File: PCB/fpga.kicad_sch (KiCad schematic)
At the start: 76 parts, among them IC1 S25FL256LAGMFI003, J1 0878311420, J4 62684-402100ALF, U4 XC7A100T-FTG256, U5 IS62C1024AL-35QLI-TR, Y2 ECS-3953M-400-BN-TR

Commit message: Add
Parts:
- removed C24, C25, C26, C27, C28, C29, C43, C44, C50, C51, C61, C62, C68, C69, C75, C76, C82, C83: 4.7u, symbol Device:C
- removed C30, C31, C32, C33, C34, C35, C36, C38, C40, C41, C45, C46, C47, C52, C53, C54, C55, C56, C58, C59, C60, C64, C65, C66, C67, C71, C72, C73, C74, C78, C79, C80, C81: 470n, symbol Device:C
- removed C37: 330u, symbol Device:C
- removed C39: 100u, symbol Device:C
- removed C42, C48, C49, C63, C70, C77, C84: 47u, symbol Device:C
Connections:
- net GND: no longer U4.L4 (IO_L1P_T0_34), U4.L5 (IO_0_34), U4.M1 (IO_L2N_T0_34), U4.M2 (IO_L2P_T0_34), U4.M4 (IO_L1N_T0_34), U4.M5 (IO_L6P_T0_34), U4.N1 (IO_L4P_T0_34), U4.N2 (IO_L3N_T0_DQS_34), U4.N3 (IO_L3P_T0_DQS_34), U4.N4 (IO_L6N_T0_VREF_34), U4.P1 (IO_L4N_T0_34), U4.P3 (IO_L5N_T0_34), U4.P4 (IO_L5P_T0_34), U4.R1 (IO_L7N_T1_34), U4.R2 (IO_L7P_T1_34), U4.R3 (IO_L8P_T1_34), U4.T2 (IO_L8N_T1_34)
- new net BLUE0: U4.P3 (IO_L5N_T0_34)
- new net BLUE1: U4.M5 (IO_L6P_T0_34)
- new net BLUE2: U4.N4 (IO_L6N_T0_VREF_34)
- new net BLUE3: U4.R2 (IO_L7P_T1_34)
- new net BLUE4: U4.R1 (IO_L7N_T1_34)
- new net GREEN0: U4.N3 (IO_L3P_T0_DQS_34)
- new net GREEN1: U4.N2 (IO_L3N_T0_DQS_34)
- new net GREEN2: U4.N1 (IO_L4P_T0_34)
- new net GREEN3: U4.P1 (IO_L4N_T0_34)
- new net GREEN4: U4.P4 (IO_L5P_T0_34)
- new net HSYNC: U4.T2 (IO_L8N_T1_34)
- new net RED0: U4.L5 (IO_0_34)
- new net RED1: U4.L4 (IO_L1P_T0_34)
- new net RED2: U4.M4 (IO_L1N_T0_34)
- new net RED3: U4.M2 (IO_L2P_T0_34)
- new net RED4: U4.M1 (IO_L2N_T0_34)
- new net VSYNC: U4.R3 (IO_L8P_T1_34)
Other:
- moved on the sheet: J4, U4B, U4D

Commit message: pls work
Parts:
- C23, C57: value C -> 100n
- R13: value R -> 2.4k
- R14, R15, R18, R19: value R -> 4.7k
- R16, R17: value R -> 10k
- R20: value R -> 330
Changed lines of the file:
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@@
       (effects (font (size 1.27 1.27)) hide)
     )
-    (property "Value" "GND" (at 262.89 100.33 0)
+    (property "Value" "GND" (at 243.205 90.17 0)
       (effects (font (size 1.27 1.27)))
     )
@@
   )
   (symbol (lib_id "Device:C") (at 35.56 33.02 90) (unit 1)
-    (in_bom yes) (on_board yes) (dnp no) (fields_autoplaced)
-    (property "Reference" "C57" (at 35.56 25.4 90)
-      (effects (font (size 1.27 1.27)))
-    )
-    (property "Value" "C" (at 35.56 27.94 90)
+    (in_bom yes) (on_board yes) (dnp no)
+    (property "Reference" "C57" (at 35.56 26.67 90)
+      (effects (font (size 1.27 1.27)))
+    )
+    (property "Value" "100n" (at 35.56 29.21 90)
       (effects (font (size 1.27 1.27)))
     )
@@
       (effects (font (size 1.27 1.27)) (justify left))
     )
-    (property "Value" "C" (at 90.17 175.895 0)
+    (property "Value" "100n" (at 90.17 175.895 0)
       (effects (font (size 1.27 1.27)) (justify left))
     )
@@
   )
   (symbol (lib_id "Device:R") (at 33.02 105.41 180) (unit 1)
-    (in_bom yes) (on_board yes) (dnp no) (fields_autoplaced)
-    (property "Reference" "R16" (at 35.56 104.14 0)
+    (in_bom yes) (on_board yes) (dnp no)
+    (property "Reference" "R16" (at 31.115 99.695 0)
       (effects (font (size 1.27 1.27)) (justify right))
     )
-    (property "Value" "R" (at 35.56 106.68 0)
+    (property "Value" "10k" (at 33.02 107.315 90)
       (effects (font (size 1.27 1.27)) (justify right))
     )
@@
   )
   (symbol (lib_id "Device:R") (at 48.26 142.24 180) (unit 1)
-    (in_bom yes) (on_board yes) (dnp no) (fields_autoplaced)
-    (property "Reference" "R19" (at 50.8 140.97 0)
+    (in_bom yes) (on_board yes) (dnp no)
+    (property "Reference" "R19" (at 50.165 140.97 0)
       (effects (font (size 1.27 1.27)) (justify right))
     )
-    (property "Value" "R" (at 50.8 143.51 0)
+    (property "Value" "4.7k" (at 48.26 144.145 90)
       (effects (font (size 1.27 1.27)) (justify right))
     )
@@
       (effects (font (size 1.27 1.27)) hide)
     )
-    (property "Value" "GND" (at 295.91 100.33 0)
+    (property "Value" "GND" (at 275.59 90.17 0)
       (effects (font (size 1.27 1.27)))
     )
@@
   )
   (symbol (lib_id "Device:R") (at 53.34 24.13 270) (unit 1)
-    (in_bom yes) (on_board yes) (dnp no) (fields_autoplaced)
+    (in_bom yes) (on_board yes) (dnp no)
     (property "Reference" "R14" (at 53.34 17.78 90)
       (effects (font (size 1.27 1.27)))
     )
-    (property "Value" "R" (at 53.34 20.32 90)
+    (property "Value" "4.7k" (at 53.34 24.13 90)
       (effects (font (size 1.27 1.27)))
     )
@@
       (effects (font (size 1.27 1.27)) hide)
     )
-    (property "Value" "GND" (at 236.22 34.29 0)
+    (property "Value" "GND" (at 241.3 32.385 0)
       (effects (font (size 1.27 1.27)))
     )
@@
   (symbol (lib_id "Device:R") (at 39.37 105.41 0) (unit 1)
     (in_bom yes) (on_board yes) (dnp no)
-    (property "Reference" "R17" (at 41.91 104.14 0)
+    (property "Reference" "R17" (at 37.465 99.695 0)
       (effects (font (size 1.27 1.27)) (justify left))
     )
-    (property "Value" "R" (at 41.91 106.68 0)
+    (property "Value" "10k" (at 39.37 107.315 90)
       (effects (font (size 1.27 1.27)) (justify left))
     )
@@
   )
   (symbol (lib_id "Device:R") (at 44.45 21.59 90) (unit 1)
-    (in_bom yes) (on_board yes) (dnp no) (fields_autoplaced)
+    (in_bom yes) (on_board yes) (dnp no)
     (property "Reference" "R13" (at 44.45 15.24 90)
       (effects (font (size 1.27 1.27)))
     )
-    (property "Value" "R" (at 44.45 17.78 90)
+    (property "Value" "2.4k" (at 44.45 21.59 90)
       (effects (font (size 1.27 1.27)))
     )
@@
       (effects (font (size 1.27 1.27)) (justify left))
     )
-    (property "Value" "R" (at 85.09 53.34 0)
+    (property "Value" "4.7k" (at 82.55 53.975 90)
       (effects (font (size 1.27 1.27)) (justify left))
     )
@@
   )
   (symbol (lib_id "Device:R") (at 50.8 109.22 180) (unit 1)
-    (in_bom yes) (on_board yes) (dnp no) (fields_autoplaced)
-    (property "Reference" "R20" (at 53.34 107.95 0)
+    (in_bom yes) (on_board yes) (dnp no)
+    (property "Reference" "R20" (at 46.99 105.41 0)
       (effects (font (size 1.27 1.27)) (justify right))
     )
-    (property "Value" "R" (at 53.34 110.49 0)
+    (property "Value" "330" (at 50.8 111.125 90)
       (effects (font (size 1.27 1.27)) (justify right))
     )
@@
   )
   (symbol (lib_id "Device:R") (at 43.18 130.81 180) (unit 1)
-    (in_bom yes) (on_board yes) (dnp no) (fields_autoplaced)
-    (property "Reference" "R18" (at 45.72 129.54 0)
+    (in_bom yes) (on_board yes) (dnp no)
+    (property "Reference" "R18" (at 44.45 130.175 0)
       (effects (font (size 1.27 1.27)) (justify right))
     )
-    (property "Value" "R" (at 45.72 132.08 0)
+    (property "Value" "4.7k" (at 43.18 132.715 90)
       (effects (font (size 1.27 1.27)) (justify right))
     )

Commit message: Footprints
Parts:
- C23, C57: footprint (none) -> Capacitor_SMD:C_0805_2012Metric_Pad1.18x1.45mm_HandSolder
- IC1: footprint (none) -> LIB_S25FL256LAGMFI003:SOIC127P1030X265-16N
- J1: footprint 0878311420 -> 0878311420_fpga-debub:0878311420
- J4: footprint 62684402100ALF -> screenconnect:62684402100ALF
- R13, R14, R15, R16, R17, R18, R19, R20: footprint (none) -> Resistor_SMD:R_0805_2012Metric_Pad1.20x1.40mm_HandSolder
- U4: footprint (none) -> fpga:BGA256C100P16X16_1700X1700X155
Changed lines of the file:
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@@
       (effects (font (size 1.27 1.27)))
     )
-    (property "Footprint" "0878311420" (at 35.56 209.22 0)
+    (property "Footprint" "0878311420_fpga-debub:0878311420" (at 35.56 209.22 0)
       (effects (font (size 1.27 1.27)) (justify left top) hide)
     )
@@
       (effects (font (size 1.27 1.27)))
     )
-    (property "Footprint" "" (at 39.37 32.0548 0)
+    (property "Footprint" "Capacitor_SMD:C_0805_2012Metric_Pad1.18x1.45mm_HandSolder" (at 39.37 32.0548 0)
       (effects (font (size 1.27 1.27)) hide)
     )
@@
       (effects (font (size 1.27 1.27)) (justify left))
     )
-    (property "Footprint" "" (at 87.3252 178.435 0)
+    (property "Footprint" "Capacitor_SMD:C_0805_2012Metric_Pad1.18x1.45mm_HandSolder" (at 87.3252 178.435 0)
       (effects (font (size 1.27 1.27)) hide)
     )
@@
       (effects (font (size 1.27 1.27)))
     )
-    (property "Footprint" "" (at 138.43 95.25 0)
+    (property "Footprint" "fpga:BGA256C100P16X16_1700X1700X155" (at 138.43 95.25 0)
       (effects (font (size 1.27 1.27)) hide)
     )
@@
       (effects (font (size 1.27 1.27)) (justify right))
     )
-    (property "Footprint" "" (at 34.798 105.41 90)
+    (property "Footprint" "Resistor_SMD:R_0805_2012Metric_Pad1.20x1.40mm_HandSolder" (at 34.798 105.41 90)
       (effects (font (size 1.27 1.27)) hide)
     )
@@
       (effects (font (size 1.27 1.27)))
     )
-    (property "Footprint" "" (at 33.02 -33.96 0)
+    (property "Footprint" "LIB_S25FL256LAGMFI003:SOIC127P1030X265-16N" (at 33.02 -33.96 0)
       (effects (font (size 1.27 1.27)) (justify left top) hide)
     )
@@
       (effects (font (size 1.27 1.27)) (justify right))
     )
-    (property "Footprint" "" (at 50.038 142.24 90)
+    (property "Footprint" "Resistor_SMD:R_0805_2012Metric_Pad1.20x1.40mm_HandSolder" (at 50.038 142.24 90)
       (effects (font (size 1.27 1.27)) hide)
     )
@@
       (effects (font (size 1.27 1.27)))
     )
-    (property "Footprint" "" (at 53.34 22.352 90)
+    (property "Footprint" "Resistor_SMD:R_0805_2012Metric_Pad1.20x1.40mm_HandSolder" (at 53.34 22.352 90)
       (effects (font (size 1.27 1.27)) hide)
     )
@@
       (effects (font (size 1.27 1.27)))
     )
-    (property "Footprint" "" (at 262.89 54.61 0)
+    (property "Footprint" "fpga:BGA256C100P16X16_1700X1700X155" (at 262.89 54.61 0)
       (effects (font (size 1.27 1.27)) hide)
     )
@@
       (effects (font (size 1.27 1.27)))
     )
-    (property "Footprint" "62684402100ALF" (at 381 242.24 0)
+    (property "Footprint" "screenconnect:62684402100ALF" (at 381 242.24 0)
       (effects (font (size 1.27 1.27)) (justify left top) hide)
     )
@@
       (effects (font (size 1.27 1.27)))
     )
-    (property "Footprint" "" (at 323.85 175.26 0)
+    (property "Footprint" "fpga:BGA256C100P16X16_1700X1700X155" (at 323.85 175.26 0)
       (effects (font (size 1.27 1.27)) hide)
     )
@@
       (effects (font (size 1.27 1.27)))
     )
-    (property "Footprint" "" (at 74.93 111.76 0)
+    (property "Footprint" "fpga:BGA256C100P16X16_1700X1700X155" (at 74.93 111.76 0)
       (effects (font (size 1.27 1.27)) hide)
     )
@@
       (effects (font (size 1.27 1.27)) (justify left))
     )
-    (property "Footprint" "" (at 37.592 105.41 90)
+    (property "Footprint" "Resistor_SMD:R_0805_2012Metric_Pad1.20x1.40mm_HandSolder" (at 37.592 105.41 90)
       (effects (font (size 1.27 1.27)) hide)
     )
@@
       (effects (font (size 1.27 1.27)))
     )
-    (property "Footprint" "" (at 44.45 23.368 90)
+    (property "Footprint" "Resistor_SMD:R_0805_2012Metric_Pad1.20x1.40mm_HandSolder" (at 44.45 23.368 90)
       (effects (font (size 1.27 1.27)) hide)
     )
@@
       (effects (font (size 1.27 1.27)) (justify left))
     )
-    (property "Footprint" "" (at 80.772 52.07 90)
+    (property "Footprint" "Resistor_SMD:R_0805_2012Metric_Pad1.20x1.40mm_HandSolder" (at 80.772 52.07 90)
       (effects (font (size 1.27 1.27)) hide)
     )
@@
       (effects (font (size 1.27 1.27)) (justify right))
     )
-    (property "Footprint" "" (at 52.578 109.22 90)
+    (property "Footprint" "Resistor_SMD:R_0805_2012Metric_Pad1.20x1.40mm_HandSolder" (at 52.578 109.22 90)
       (effects (font (size 1.27 1.27)) hide)
     )
@@
       (effects (font (size 1.27 1.27)) (justify right))
     )
-    (property "Footprint" "" (at 44.958 130.81 90)
-      (effects (font (size 1.27 1.27)) hide)
-    )
+    (property "Footprint" "Resistor_SMD:R_0805_2012Metric_Pad1.20x1.40mm_HandSolder" (at 44.958 130.81 90)
+      (effects (font (size 1.27 1.27)) hide)
+    )

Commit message: more
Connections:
- net at J1.4, R16.2, U4.M7 (TMS_0): no longer R17.1
- net at J1.6, U4.L7 (TCK_0): now also R17.1
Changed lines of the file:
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@@
   (junction (at 240.03 52.07) (diameter 0) (color 0 0 0 0)
   )
+  (junction (at 41.91 119.38) (diameter 0) (color 0 0 0 0)
+  )
   (junction (at 374.65 127) (diameter 0) (color 0 0 0 0)
   )
@@
   )
   (junction (at 93.98 77.47) (diameter 0) (color 0 0 0 0)
-  )
-  (junction (at 41.91 116.84) (diameter 0) (color 0 0 0 0)
   )
   (junction (at 167.64 87.63) (diameter 0) (color 0 0 0 0)
@@
     (stroke (width 0) (type default))
   )
-  (wire (pts (xy 35.56 116.84) (xy 41.91 116.84))
+  (wire (pts (xy 35.56 116.84) (xy 58.42 116.84))
     (stroke (width 0) (type default))
   )
@@
     (stroke (width 0) (type default))
   )
-  (wire (pts (xy 41.91 116.84) (xy 58.42 116.84))
-    (stroke (width 0) (type default))
-  )
   (wire (pts (xy 62.23 121.92) (xy 67.31 121.92))
     (stroke (width 0) (type default))
@@
     (stroke (width 0) (type default))
   )
-  (wire (pts (xy 33.02 119.38) (xy 55.88 119.38))
+  (wire (pts (xy 33.02 119.38) (xy 41.91 119.38))
     (stroke (width 0) (type default))
   )
@@
     (stroke (width 0) (type default))
   )
+  (wire (pts (xy 41.91 119.38) (xy 55.88 119.38))
+    (stroke (width 0) (type default))
+  )
   (wire (pts (xy 40.64 163.195) (xy 40.64 170.18))
     (stroke (width 0) (type default))
@@
     (stroke (width 0) (type default))
   )
-  (wire (pts (xy 41.91 101.6) (xy 41.91 116.84))
-    (stroke (width 0) (type default))
-  )
   (wire (pts (xy 15.24 134.62) (xy 15.24 129.54))
     (stroke (width 0) (type default))
@@
     (stroke (width 0) (type default))
   )
+  (wire (pts (xy 41.91 101.6) (xy 41.91 119.38))
+    (stroke (width 0) (type default))
+  )

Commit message: schematic fixes
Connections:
- net GND: no longer U4.A13 (IO_L7P_T1_AD2P_15), U4.A14 (IO_L7N_T1_AD2N_15), U4.A15 (IO_L9N_T1_DQS_AD3N_15), U4.A3 (IO_L4N_T0_35), U4.A4 (IO_L3N_T0_DQS_AD5N_35), U4.A5 (IO_L3P_T0_DQS_AD5P_35), U4.A7 (IO_L1N_T0_AD4N_35), U4.B14 (IO_L8N_T1_AD10N_15), U4.B15 (IO_L9P_T1_DQS_AD3P_15), U4.B16 (IO_L10N_T1_AD11N_15), U4.B4 (IO_L4P_T0_35), U4.B5 (IO_L2N_T0_AD12N_35), U4.B6 (IO_L2P_T0_AD12P_35), U4.B7 (IO_L1P_T0_AD4P_35), U4.C14 (IO_L8P_T1_AD10P_15), U4.C16 (IO_L10P_T1_AD11P_15), U4.C7 (IO_L5P_T0_AD13P_35), U4.D9 (IO_L6N_T0_VREF_15), U4.E6 (IO_0_35), U4.K13 (IO_L5P_T0_D06_14), U4.L13 (IO_L5N_T0_D07_14), U4.L14 (IO_L4P_T0_D04_14), U4.M12 (IO_L6N_T0_D08_VREF_14), U4.M14 (IO_L4N_T0_D05_14), U4.M15 (IO_L3N_T0_DQS_EMCCLK_14), U4.M16 (IO_L7P_T1_D09_14), U4.M6 (IO_L19P_T3_A10_D26_14), U4.N12 (IO_L13N_T2_MRCC_14), U4.N13 (IO_L11P_T1_SRCC_14), U4.N14 (IO_L12P_T1_MRCC_14), U4.N16 (IO_L7N_T1_D10_14), U4.N6 (IO_L19N_T3_A09_D25_VREF_14), U4.N9 (IO_L18P_T2_A12_D28_14), U4.P10 (IO_L14P_T2_SRCC_14), U4.P11 (IO_L14N_T2_SRCC_14), U4.P13 (IO_L11N_T1_SRCC_14), U4.P14 (IO_L12N_T1_MRCC_14), U4.P15 (IO_L8P_T1_D11_14), U4.P16 (IO_L8N_T1_D12_14), U4.P5 (IO_L10P_T1_34), U4.P6 (IO_25_14), U4.P8 (IO_L20P_T3_A08_D24_14), U4.P9 (IO_L18N_T2_A11_D27_14), U4.R10 (IO_L17P_T2_A14_D30_14), U4.R11 (IO_L17N_T2_A13_D29_14), U4.R12 (IO_L15P_T2_DQS_RDWR_B_14), U4.R13 (IO_L16P_T2_CSI_B_14), U4.R15 (IO_L9P_T1_DQS_14), U4.R16 (IO_L9N_T1_DQS_D13_14), U4.R5 (IO_L23P_T3_A03_D19_14), U4.R6 (IO_L24P_T3_A01_D17_14), U4.R7 (IO_L24N_T3_A00_D16_14), U4.R8 (IO_L20N_T3_A07_D23_14), U4.T10 (IO_L22N_T3_A04_D20_14), U4.T12 (IO_L15N_T2_DQS_DOUT_CSO_B_14), U4.T13 (IO_L16N_T2_A15_D31_14), U4.T14 (IO_L10P_T1_D14_14), U4.T15 (IO_L10N_T1_D15_14), U4.T3 (IO_L9N_T1_DQS_34), U4.T4 (IO_L9P_T1_DQS_34), U4.T5 (IO_L23N_T3_A02_D18_14), U4.T7 (IO_L21P_T3_DQS_14), U4.T8 (IO_L21N_T3_DQS_A06_D22_14), U4.T9 (IO_L22P_T3_A05_D21_14)
- no-connect marks 13 -> 77

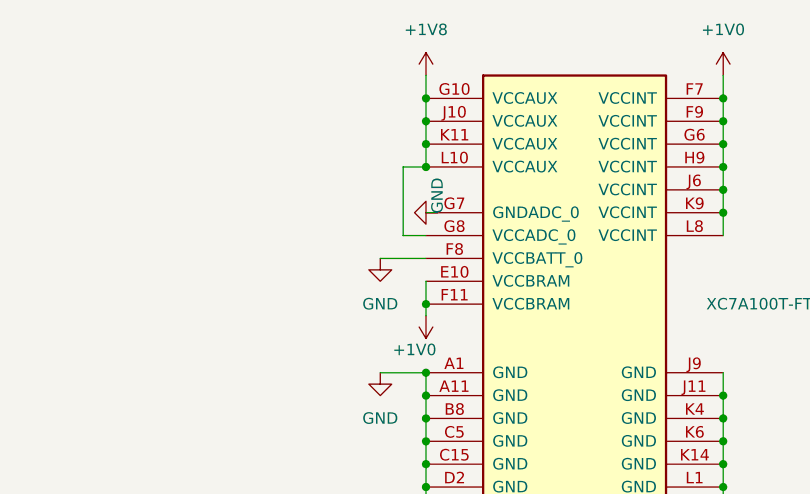
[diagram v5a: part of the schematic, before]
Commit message: schematic fixes.2
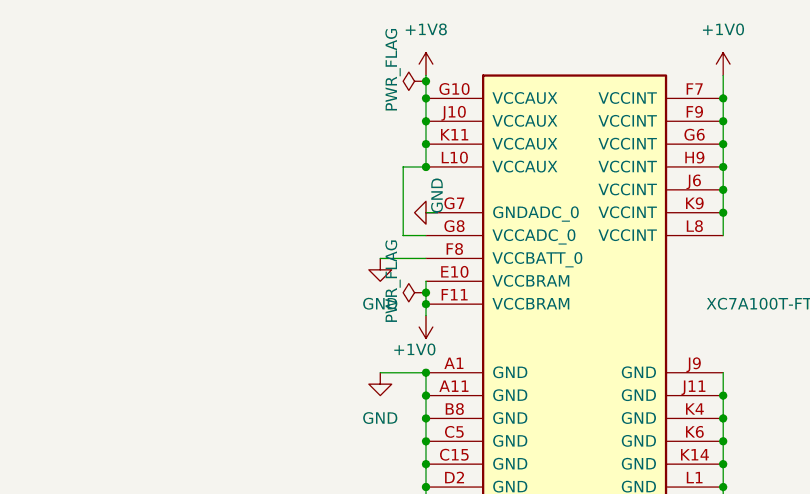
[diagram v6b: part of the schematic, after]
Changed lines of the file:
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@@
   (junction (at 106.68 21.59) (diameter 0) (color 0 0 0 0)
   )
+  (junction (at 240.03 43.18) (diameter 0) (color 0 0 0 0)
+  )
   (junction (at 273.05 31.75) (diameter 0) (color 0 0 0 0)
   )
@@
   )
   (junction (at 147.32 21.59) (diameter 0) (color 0 0 0 0)
+  )
+  (junction (at 240.03 19.685) (diameter 0) (color 0 0 0 0)
   )
   (junction (at 15.24 116.84) (diameter 0) (color 0 0 0 0)
@@
     (stroke (width 0) (type default))
   )
+  (wire (pts (xy 240.03 43.18) (xy 240.03 44.45))
+    (stroke (width 0) (type default))
+  )
   (wire (pts (xy 62.23 121.92) (xy 67.31 121.92))
     (stroke (width 0) (type default))
@@
     (stroke (width 0) (type default))
   )
-  (wire (pts (xy 240.03 19.05) (xy 240.03 21.59))
+  (wire (pts (xy 240.03 19.05) (xy 240.03 19.685))
     (stroke (width 0) (type default))
   )
@@
     (stroke (width 0) (type default))
   )
-  (wire (pts (xy 240.03 41.91) (xy 240.03 44.45))
+  (wire (pts (xy 240.03 41.91) (xy 240.03 43.18))
     (stroke (width 0) (type default))
   )
@@
   )
   (wire (pts (xy 222.25 123.19) (xy 167.64 123.19))
+    (stroke (width 0) (type default))
+  )
+  (wire (pts (xy 240.03 19.685) (xy 240.03 21.59))
     (stroke (width 0) (type default))
   )
@@
         (path "/aa113cd6-c3ac-4890-9a84-1ea195994408/e43e14ef-0971-4dbf-9758-48ad88cea06a"
           (reference "J1") (unit 1)
+        )
+      )
+    )
+  )
+  (symbol (lib_id "power:PWR_FLAG") (at 240.03 19.685 90) (unit 1)
+    (in_bom yes) (on_board yes) (dnp no)
+    (property "Reference" "#FLG01" (at 238.125 19.685 0)
+      (effects (font (size 1.27 1.27)) hide)
+    )
+    (property "Value" "PWR_FLAG" (at 236.22 18.415 0)
+      (effects (font (size 1.27 1.27)))
+    )
+    (property "Footprint" "" (at 240.03 19.685 0)
+      (effects (font (size 1.27 1.27)) hide)
+    )
+    (property "Datasheet" "~" (at 240.03 19.685 0)
+      (effects (font (size 1.27 1.27)) hide)
+    )
+    (pin "1")
+    (instances
+      (project "PCB"
+        (path "/aa113cd6-c3ac-4890-9a84-1ea195994408/6d6ebb76-19de-41e4-9a7d-528f4e5c1c0f"
+          (reference "#FLG01") (unit 1)
+        )
+        (path "/aa113cd6-c3ac-4890-9a84-1ea195994408/e43e14ef-0971-4dbf-9758-48ad88cea06a"
+          (reference "#FLG04") (unit 1)
         )
       )
@@
         )
       )
+    )
+  )
+  (symbol (lib_id "power:PWR_FLAG") (at 240.03 43.18 90) (unit 1)
+    (in_bom yes) (on_board yes) (dnp no)
+    (property "Reference" "#FLG01" (at 238.125 43.18 0)
+      (effects (font (size 1.27 1.27)) hide)
+    )
+    (property "Value" "PWR_FLAG" (at 236.22 41.91 0)
+      (effects (font (size 1.27 1.27)))
+    )
+    (property "Footprint" "" (at 240.03 43.18 0)
+      (effects (font (size 1.27 1.27)) hide)
+    )
+    (property "Datasheet" "~" (at 240.03 43.18 0)
+      (effects (font (size 1.27 1.27)) hide)
+    )
+    (pin "1")
+    (instances
+      (project "PCB"
+        (path "/aa113cd6-c3ac-4890-9a84-1ea195994408/6d6ebb76-19de-41e4-9a7d-528f4e5c1c0f"
+          (reference "#FLG01") (unit 1)
+        )
+        (path "/aa113cd6-c3ac-4890-9a84-1ea195994408/e43e14ef-0971-4dbf-9758-48ad88cea06a"
+          (reference "#FLG03") (unit 1)
+        )
+      )

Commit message: PCB
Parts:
- added C95: 4.7u, Capacitor_SMD:C_0805_2012Metric_Pad1.18x1.45mm_HandSolder, symbol Device:C
- added C96: 1u, Capacitor_SMD:C_0805_2012Metric_Pad1.18x1.45mm_HandSolder, symbol Device:C
- added D2: MBR0520, Diode_SMD:D_SOD-123, symbol Diode:MBR0520
- added IC2: LT1932ES6#TRMPBF, ledDriver:SOT95P280X100-6N, symbol LT1932ES6#TRMPBF:LT1932ES6#TRMPBF
- added L4: 6.8u, Inductor_SMD:L_0805_2012Metric_Pad1.05x1.20mm_HandSolder, symbol Device:L
- added R40: 562, Resistor_SMD:R_0805_2012Metric_Pad1.20x1.40mm_HandSolder, symbol Device:R
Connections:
- net +3.3V: now also J4.4, C95.1, IC2.5 (~{SHDN}), IC2.6 (VIN), L4.1
- net GND: now also J4.29, C95.2, C96.2, IC2.2 (GND), R40.2
- net at J4.1: now also IC2.3 (LED); no longer U4.C6 (IO_L5N_T0_AD13N_35)
- net at J4.2: now also C96.1, D2.1 (K); no longer U4.D6 (IO_L6P_T0_35)
- net at U4.J4 (IO_L19N_T3_VREF_35): no longer J4.29
- net at U4.C3 (IO_L7P_T1_AD6P_35): no longer J4.4
- new net: IC2.4 (RSET), R40.1
- new net: D2.2 (A), IC2.1 (SW), L4.2
- no-connect marks 77 -> 81
